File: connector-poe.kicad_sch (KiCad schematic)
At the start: 29 parts, among them J101 2x05_Horizontal, J102 NE8FAH, J103 JAE_DX07S016JA3, J104 2x05_Horizontal, J105 NE8FAH, J106 WAGO-2065, J107 WAGO-2065, J108 WAGO-2065, J109 WAGO-2065

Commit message: Rename to connector-poe
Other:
- title: V2 power RJ45 -> V2 connector PoE
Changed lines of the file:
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@@
 	(paper "A4")
 	(title_block
-		(title "V2 power RJ45")
-		(date "2024-06-20")
+		(title "V2 connector PoE")
+		(date "2024-07-04")
 		(rev "4")
 		(company "Versio Duo")
-		(comment 1 "Power Supply")
+		(comment 1 "V2 Link  + PoE Mode B")
 	)
 	(junction
@@
 		(at 187.96 179.07 0)
 		(unit 1)
-		(exclude_from_sim no)
+		(exclude_from_sim yes)
 		(in_bom no)
 		(on_board yes)
@@
 			)
 		)
-		(property "Sim.Enable" "0"
-			(at 187.96 179.07 0)
-			(effects
-				(font
-					(size 1.27 1.27)
-				)
-				(hide yes)
-			)
-		)
 		(instances
 			(project ""
@@
 		(at 187.96 173.99 0)
 		(unit 1)
-		(exclude_from_sim no)
+		(exclude_from_sim yes)
 		(in_bom no)
 		(on_board yes)
@@
 			(at 187.96 173.99 0)
 			(effects
-				(font
-					(size 1.27 1.27)
-				)
-				(hide yes)
-			)
-		)
-		(property "Sim.Enable" "0"
-			(at 187.96 173.99 0)
-			(effects

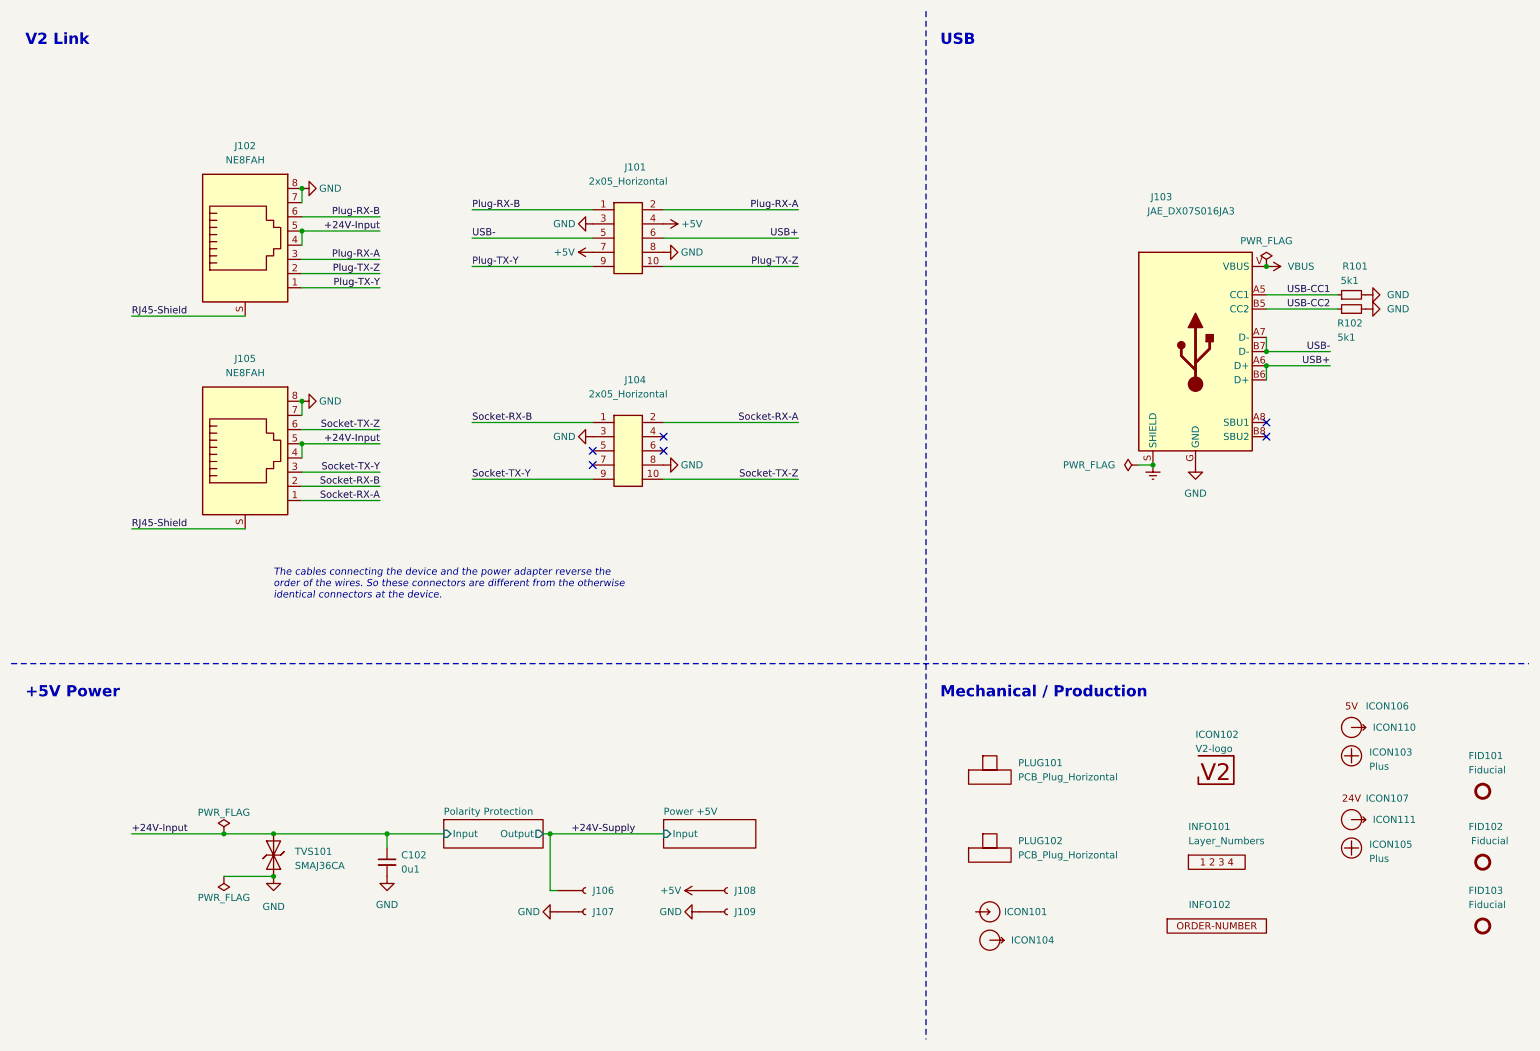
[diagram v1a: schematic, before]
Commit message: Back-to-back Mosfet
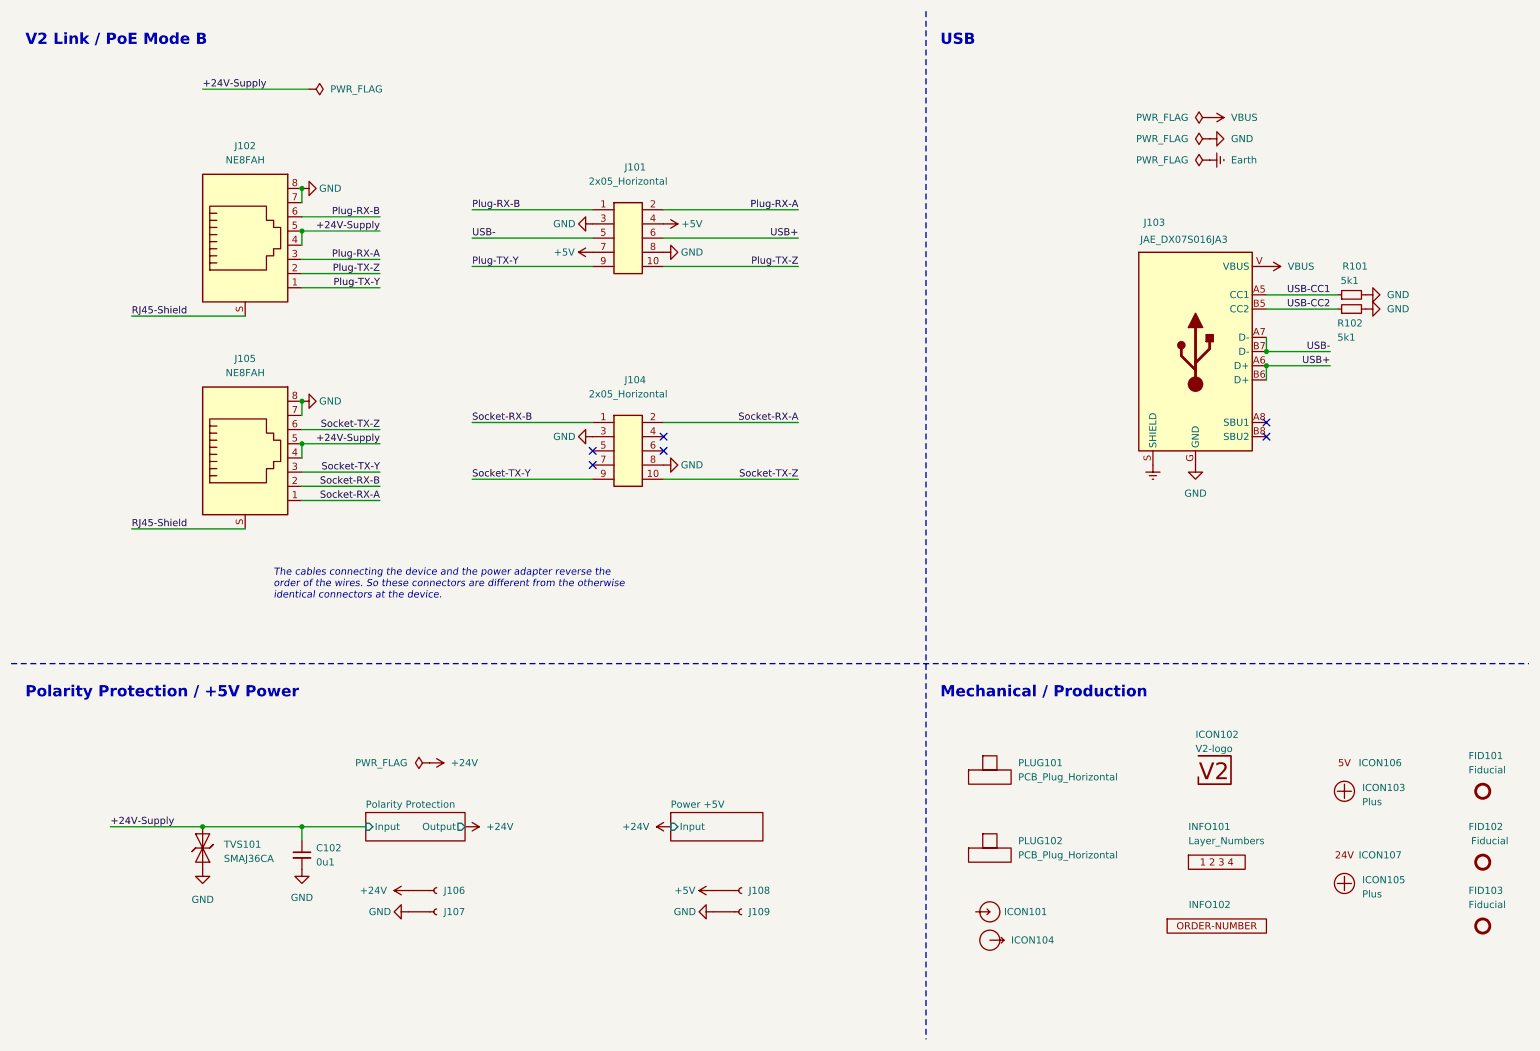
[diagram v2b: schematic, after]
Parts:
- removed ICON110, ICON111: Arrow_Out, V2_Artwork:Arrow_Out, symbol V2_Artwork:Arrow_Out
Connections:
- net +24V-Input is gone; now on net +24V-Supply: C102.1, J102.4, J102.5, J105.4, J105.5, TVS101.2 (A)
- net +24V-Supply: no longer J106.1
- new net +24V: J106.1
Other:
- note added: "Polarity Protection / +5V Power"
- note added: "V2 Link / PoE Mode B"
- note removed: "+5V Power"
- note removed: "V2 Link"
- moved on the sheet: C102, ICON103, ICON105, ICON106, ICON107, J106, J107, J108, J109, TVS101
